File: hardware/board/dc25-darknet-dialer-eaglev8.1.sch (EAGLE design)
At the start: 94 parts, among them J1 MF-CON-MICROUSB-RIGHT, SW1 RESET, U1 BU33SD5WG-TR, U2 MCP73831T-5ACI/OT, U3 SOP22FLAT, Y1 CSTCE8M00G52-R0

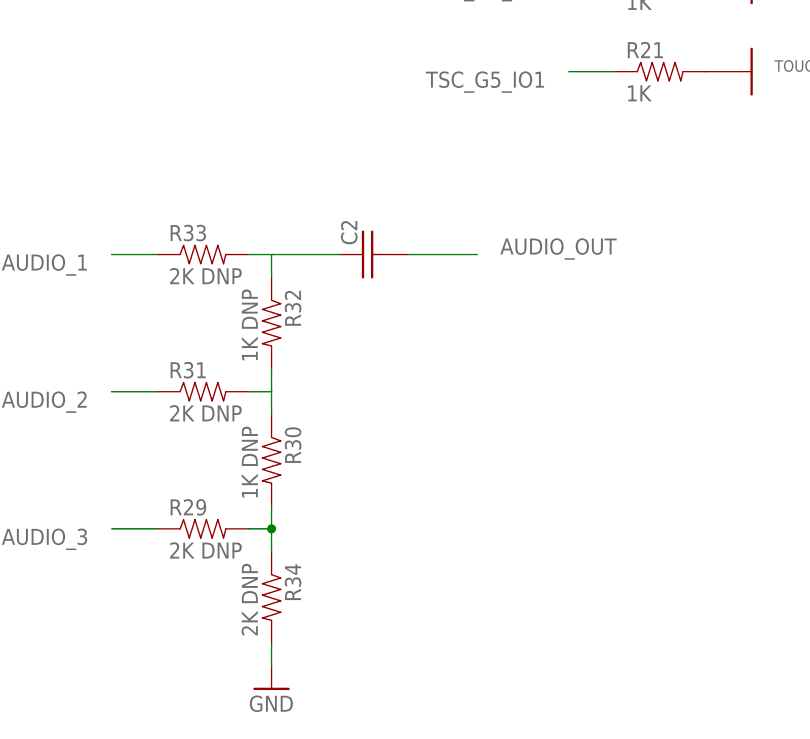
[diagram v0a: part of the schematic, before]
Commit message: Added audio out pads
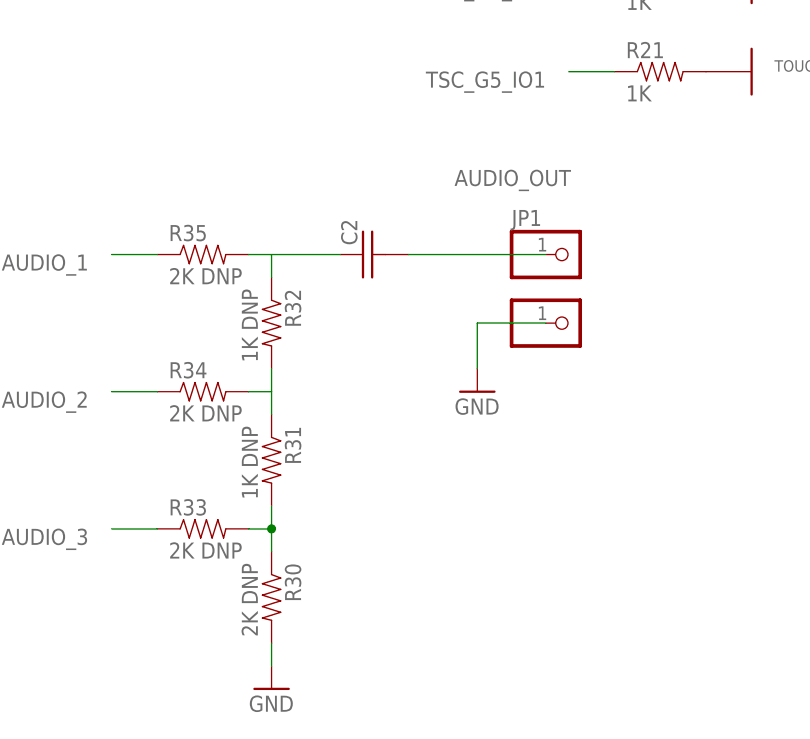
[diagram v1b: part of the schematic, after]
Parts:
- removed R29: 2K DNP, darknet_parts_library:RESISTOR0603-RES
- added JP1, JP2: (no value), adafruit:PINHD-1X1CB
- added R35: 2K DNP, darknet_parts_library:RESISTOR0603-RES
- R30: value 1K DNP -> 2K DNP
- R31: value 2K DNP -> 1K DNP
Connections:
- net AUDIO_1: now also R35.1; no longer R33.1
- net AUDIO_2: now also R34.1; no longer R31.1
- net AUDIO_3: now also R33.1; no longer R29.1
- net AUDIO_OUT: now also JP1.1
- net GND: now also JP2.1, R30.2; no longer R34.2
- net N$33: now also R35.2; no longer R33.2
- net N$34: now also R31.1, R34.2; no longer R30.1, R31.2
- net N$35: now also R30.1, R31.2, R33.2; no longer R29.2, R30.2, R34.1
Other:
- moved on the sheet: R30, R31, R33, R34
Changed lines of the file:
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@@
 <part name="J1" library="MF_Connectors" deviceset="USB" device="_MICRO_RIGHT" value="MF-CON-MICROUSB-RIGHT"/>
 <part name="U$11" library="darknet_parts_library" deviceset="SWITCH_SPDT" device=""/>
-<part name="R29" library="darknet_parts_library" deviceset="RESISTOR" device="0603-RES" value="2K DNP"/>
-<part name="R30" library="darknet_parts_library" deviceset="RESISTOR" device="0603-RES" value="1K DNP"/>
-<part name="R31" library="darknet_parts_library" deviceset="RESISTOR" device="0603-RES" value="2K DNP"/>
+<part name="R33" library="darknet_parts_library" deviceset="RESISTOR" device="0603-RES" value="2K DNP"/>
+<part name="R31" library="darknet_parts_library" deviceset="RESISTOR" device="0603-RES" value="1K DNP"/>
+<part name="R34" library="darknet_parts_library" deviceset="RESISTOR" device="0603-RES" value="2K DNP"/>
 <part name="R32" library="darknet_parts_library" deviceset="RESISTOR" device="0603-RES" value="1K DNP"/>
-<part name="R33" library="darknet_parts_library" deviceset="RESISTOR" device="0603-RES" value="2K DNP"/>
+<part name="R35" library="darknet_parts_library" deviceset="RESISTOR" device="0603-RES" value="2K DNP"/>
 <part name="C2" library="darknet_parts_library" deviceset="C-US" device="C0603" value="10uF DNP"/>
-<part name="R34" library="darknet_parts_library" deviceset="RESISTOR" device="0603-RES" value="2K DNP"/>
+<part name="R30" library="darknet_parts_library" deviceset="RESISTOR" device="0603-RES" value="2K DNP"/>
 <part name="GND17" library="SYNShop" deviceset="GND" device=""/>
+<part name="GND18" library="SYNShop" deviceset="GND" device=""/>
+<part name="JP1" library="adafruit" deviceset="PINHD-1X1" device="CB"/>
+<part name="JP2" library="adafruit" deviceset="PINHD-1X1" device="CB"/>
 </parts>
 <sheets>
@@
 <instance part="J1" gate="G$1" x="134.62" y="340.36" rot="R180"/>
 <instance part="U$11" gate="G$1" x="93.98" y="386.08"/>
-<instance part="R29" gate="G$1" x="256.54" y="7.62"/>
-<instance part="R30" gate="G$1" x="264.16" y="15.24" rot="R270"/>
-<instance part="R31" gate="G$1" x="256.54" y="22.86"/>
+<instance part="R33" gate="G$1" x="256.54" y="7.62"/>
+<instance part="R31" gate="G$1" x="264.16" y="15.24" rot="R270"/>
+<instance part="R34" gate="G$1" x="256.54" y="22.86"/>
 <instance part="R32" gate="G$1" x="264.16" y="30.48" rot="R270"/>
-<instance part="R33" gate="G$1" x="256.54" y="38.1"/>
+<instance part="R35" gate="G$1" x="256.54" y="38.1"/>
 <instance part="C2" gate="G$1" x="274.32" y="38.1" smashed="yes" rot="R90">
 <attribute name="NAME" x="273.685" y="39.116" size="1.778" layer="95" rot="R90"/>
 </instance>
-<instance part="R34" gate="G$1" x="264.16" y="0" rot="R270"/>
+<instance part="R30" gate="G$1" x="264.16" y="0" rot="R270"/>
 <instance part="GND17" gate="1" x="264.16" y="-10.16"/>
+<instance part="GND18" gate="1" x="287.02" y="22.86"/>
+<instance part="JP1" gate="G$1" x="297.18" y="38.1"/>
+<instance part="JP2" gate="G$1" x="297.18" y="30.48" smashed="yes">
+<attribute name="VALUE" x="290.83" y="25.4" size="1.778" layer="96"/>
+</instance>
 </instances>
 <busses>
@@
 </segment>
 <segment>
-<pinref part="R34" gate="G$1" pin="2"/>
+<pinref part="R30" gate="G$1" pin="2"/>
 <wire x1="264.16" y1="-5.08" x2="264.16" y2="-7.62" width="0.1524" layer="91"/>
 <pinref part="GND17" gate="1" pin="GND"/>
+</segment>
+<segment>
+<wire x1="294.64" y1="30.48" x2="287.02" y2="30.48" width="0.1524" layer="91"/>
+<wire x1="287.02" y1="30.48" x2="287.02" y2="25.4" width="0.1524" layer="91"/>
+<pinref part="GND18" gate="1" pin="GND"/>
+<pinref part="JP2" gate="G$1" pin="1"/>
 </segment>
 </net>
@@
 </segment>
 <segment>
-<pinref part="R33" gate="G$1" pin="1"/>
+<pinref part="R35" gate="G$1" pin="1"/>
 <wire x1="251.46" y1="38.1" x2="246.38" y2="38.1" width="0.1524" layer="91"/>
 <label x="243.84" y="38.1" size="1.778" layer="95" rot="R180"/>
@@
 </segment>
 <segment>
-<pinref part="R29" gate="G$1" pin="1"/>
+<pinref part="R33" gate="G$1" pin="1"/>
 <wire x1="251.46" y1="7.62" x2="246.38" y2="7.62" width="0.1524" layer="91"/>
 <label x="243.84" y="7.62" size="1.778" layer="95" rot="R180"/>
@@
 </segment>
 <segment>
-<pinref part="R31" gate="G$1" pin="1"/>
+<pinref part="R34" gate="G$1" pin="1"/>
 <wire x1="251.46" y1="22.86" x2="246.38" y2="22.86" width="0.1524" layer="91"/>
 <label x="243.84" y="22.86" size="1.778" layer="95" rot="R180"/>
@@
 <net name="N$33" class="0">
 <segment>
-<pinref part="R33" gate="G$1" pin="2"/>
+<pinref part="R35" gate="G$1" pin="2"/>
 <pinref part="C2" gate="G$1" pin="1"/>
 <wire x1="261.62" y1="38.1" x2="264.16" y2="38.1" width="0.1524" layer="91"/>
@@
 <segment>
 <pinref part="R32" gate="G$1" pin="2"/>
-<pinref part="R30" gate="G$1" pin="1"/>
+<pinref part="R31" gate="G$1" pin="1"/>
 <wire x1="264.16" y1="25.4" x2="264.16" y2="22.86" width="0.1524" layer="91"/>
-<pinref part="R31" gate="G$1" pin="2"/>
+<pinref part="R34" gate="G$1" pin="2"/>
 <wire x1="264.16" y1="22.86" x2="264.16" y2="20.32" width="0.1524" layer="91"/>
 <wire x1="261.62" y1="22.86" x2="264.16" y2="22.86" width="0.1524" layer="91"/>
@@
 <net name="N$35" class="0">
 <segment>
-<pinref part="R30" gate="G$1" pin="2"/>
+<pinref part="R31" gate="G$1" pin="2"/>
 <wire x1="264.16" y1="10.16" x2="264.16" y2="7.62" width="0.1524" layer="91"/>
-<pinref part="R29" gate="G$1" pin="2"/>
+<pinref part="R33" gate="G$1" pin="2"/>
 <wire x1="264.16" y1="7.62" x2="261.62" y2="7.62" width="0.1524" layer="91"/>
-<pinref part="R34" gate="G$1" pin="1"/>
+<pinref part="R30" gate="G$1" pin="1"/>
 <wire x1="264.16" y1="5.08" x2="264.16" y2="7.62" width="0.1524" layer="91"/>
 <junction x="264.16" y="7.62"/>
@@
 <segment>
 <pinref part="C2" gate="G$1" pin="2"/>
-<wire x1="279.4" y1="38.1" x2="287.02" y2="38.1" width="0.1524" layer="91"/>
-<label x="289.56" y="38.1" size="1.778" layer="95"/>
-</segment>
-</net>
+<wire x1="279.4" y1="38.1" x2="294.64" y2="38.1" width="0.1524" layer="91"/>
+<label x="284.48" y="45.72" size="1.778" layer="95"/>
+<pinref part="JP1" gate="G$1" pin="1"/>
+</segment>
+</net>

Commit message: Updated switch hook, and removed solder paste for kit parts
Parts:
- LED1, LED10, LED2, LED3, LED4, LED5, LED6, LED7, LED8, LED9: device SYNShop:LEDREVERSEMOUNT -> darknet_parts_library:LEDREVERSEMOUNT_NOPASTE
- U$15: value RFM69HCWRFN69HCWSMD -> RFM69HCWRFM69HCWSMDNOPASTE; device SYNShop:RFM69HCWRFN69HCWSMD -> SYNShop:RFM69HCWRFM69HCWSMDNOPASTE
